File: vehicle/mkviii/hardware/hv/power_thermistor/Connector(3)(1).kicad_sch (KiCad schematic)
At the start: 1 part, among them J4 T2M-110-01-X-D-TH-WT

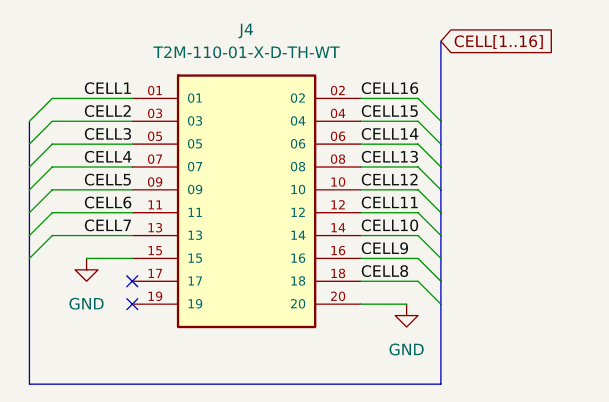
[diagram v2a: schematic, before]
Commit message: fixes for connector to BMS MOBO
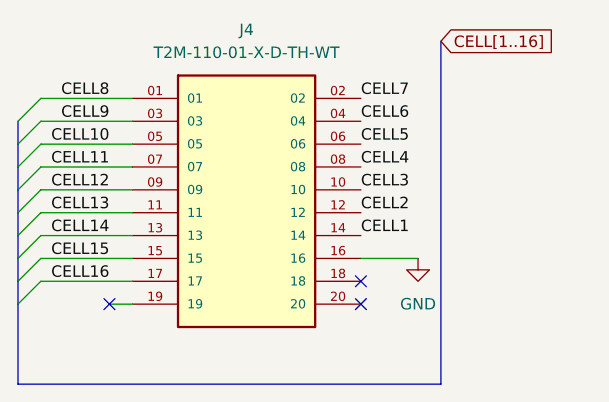
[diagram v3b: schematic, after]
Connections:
- net CELL1: now also J4.14; no longer J4.01
- net CELL10: now also J4.05; no longer J4.14
- net CELL11: now also J4.07; no longer J4.12
- net CELL12: now also J4.09; no longer J4.10
- net CELL13: now also J4.11; no longer J4.08
- net CELL14: now also J4.13; no longer J4.06
- net CELL15: now also J4.15; no longer J4.04
- net CELL16: now also J4.17; no longer J4.02
- net CELL2: now also J4.12; no longer J4.03
- net CELL3: now also J4.10; no longer J4.05
- net CELL4: now also J4.08; no longer J4.07
- net CELL5: now also J4.06; no longer J4.09
- net CELL6: now also J4.04; no longer J4.11
- net CELL7: now also J4.02; no longer J4.13
- net CELL8: now also J4.01; no longer J4.18
- net CELL9: now also J4.03; no longer J4.16
- net GND: now also J4.16; no longer J4.15, J4.20
- no-connect marks 2 -> 3
